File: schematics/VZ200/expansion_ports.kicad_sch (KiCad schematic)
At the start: 2 parts, among them P1 I/O Expansion, P2 Memory Expansion

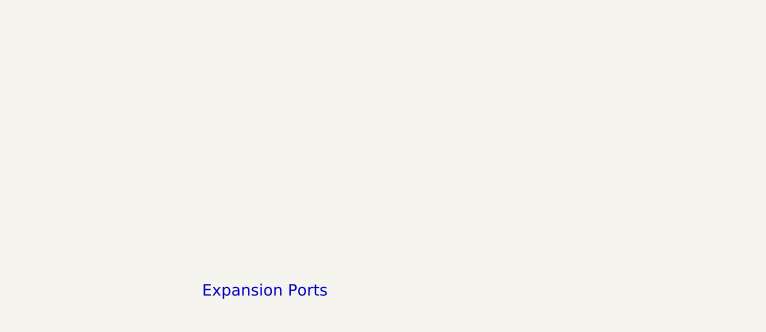
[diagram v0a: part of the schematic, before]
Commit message: Schematic for the VZ200 printer interface
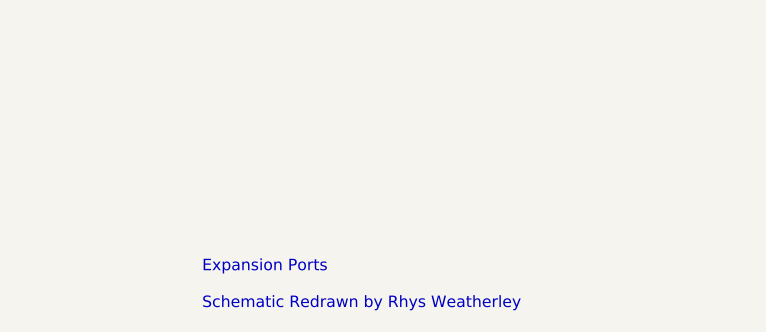
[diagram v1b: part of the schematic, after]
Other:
- note added: "Expansion Ports Schematic Redrawn by Rhys Weatherley"
- note removed: "Expansion Ports"
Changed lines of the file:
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@@
     (stroke (width 0) (type default))
   )
-  (text "Expansion Ports" (at 185.42 175.26 0)
+  (text "Expansion Ports\n\nSchematic Redrawn by Rhys Weatherley"
+    (at 185.42 176.53 0)
     (effects (font (size 1.27 1.27)) (justify left bottom))
   )

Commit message: Add title and revision details to the schematic sheets
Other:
- title: (none) -> VZ200 Computer
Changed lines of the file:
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@@
 (kicad_sch (version 20230121) (generator eeschema)
   (paper "A4")
+  (title_block
+    (title "VZ200 Computer")
+    (date "2024-01-01")
+    (rev "1")
+  )
   (junction (at 58.42 39.37) (diameter 0) (color 0 0 0 0)
   )
